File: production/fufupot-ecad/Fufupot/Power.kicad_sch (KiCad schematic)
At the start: 1 part, among them J1 Conn_01x03

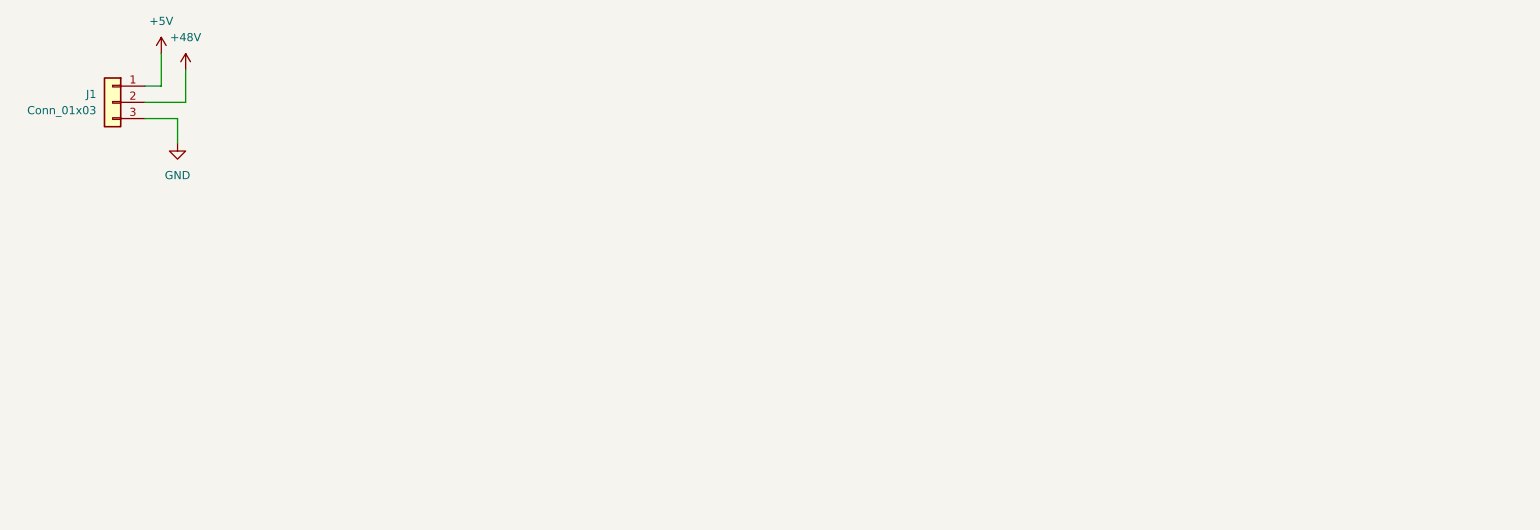
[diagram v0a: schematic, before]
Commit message: Buck Schematic
First version of my buck schematic
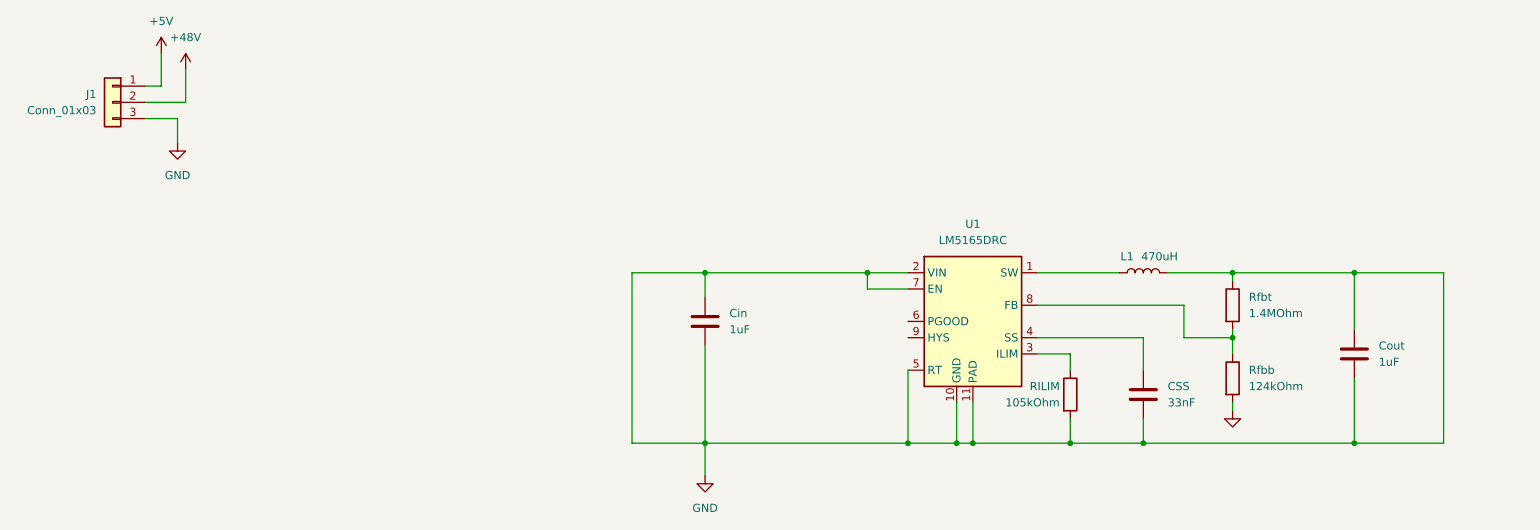
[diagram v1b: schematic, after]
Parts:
- added CSS: 33nF, symbol Device:C
- added Cin, Cout: 1uF, symbol Device:C
- added L1: 470uH, symbol Device:L
- added RILIM: 105kOhm, symbol Device:R
- added Rfbb: 124kOhm, symbol Device:R
- added Rfbt: 1.4MOhm, symbol Device:R
- added U1: LM5165DRC, Package_SON:Texas_S-PVSON-N10_ThermalVias, symbol Regulator_Switching:LM5165
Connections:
- net GND: now also CSS.2, Cin.1, Cin.2, Cout.1, Cout.2, L1.2, RILIM.2, Rfbb.2, Rfbt.1, U1.10 (GND), U1.11 (PAD), U1.2 (VIN), U1.5 (RT), U1.7 (EN)
- new net: L1.1, U1.1 (SW)
- new net: CSS.1, U1.4 (SS)
- new net: Rfbb.1, Rfbt.2, U1.8 (FB)
- new net: RILIM.1, U1.3 (ILIM)

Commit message: Input and Output
Created labels that represent the input 48V from source and where the output 15V should be.
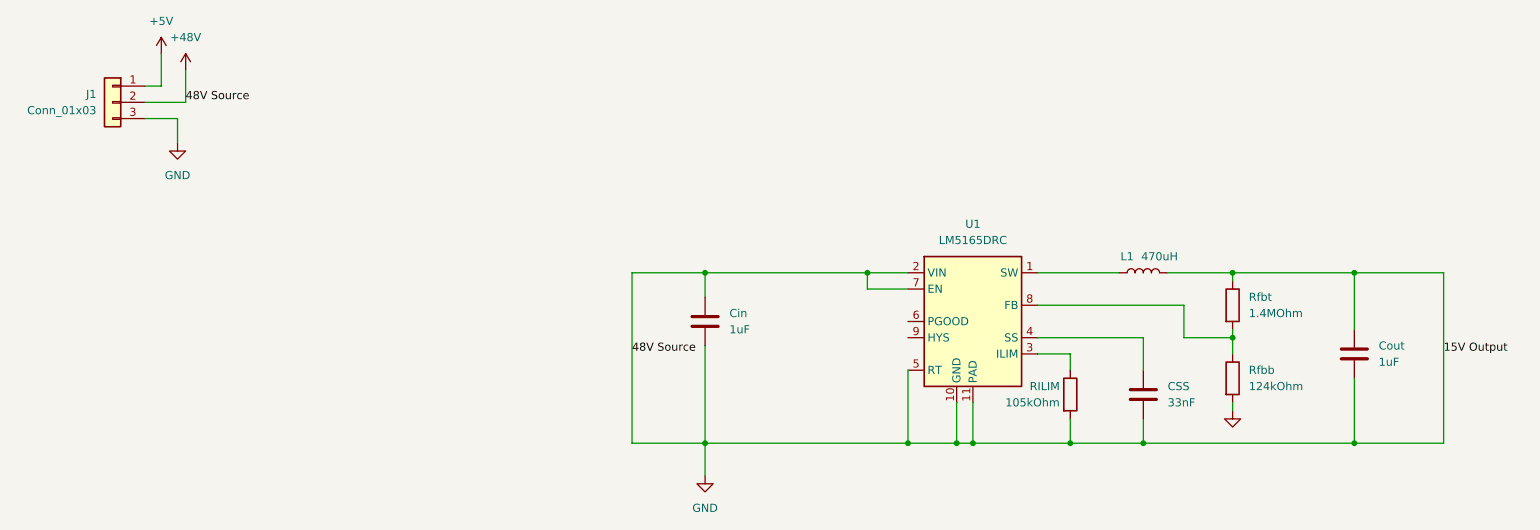
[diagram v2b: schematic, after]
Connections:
- net GND is gone; now on net +48V: CSS.2, Cin.1, Cin.2, Cout.1, Cout.2, J1.3 (Pin_3), L1.2, RILIM.2, Rfbb.2, Rfbt.1, U1.10 (GND), U1.11 (PAD), U1.2 (VIN), U1.5 (RT), U1.7 (EN)
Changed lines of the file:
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@@
+    (stroke (width 0) (type default))
+  )
+  (wire (pts (xy 128.27 68.58) (xy 128.27 95.25))
     (stroke (width 0) (type default))
   )
@@
   )
   (wire (pts (xy 57.15 44.45) (xy 52.07 44.45))
-    (stroke (width 0) (type default))
-  )
-  (wire (pts (xy 128.27 95.25) (xy 128.27 68.58))
     (stroke (width 0) (type default))
   )
@@
     (stroke (width 0) (type default))
   )
+  (label "48V Source" (at 58.42 41.91 0) (fields_autoplaced)
+    (effects (font (size 1.27 1.27)) (justify left bottom))
+  )
+  (label "15V Output" (at 255.27 81.28 0) (fields_autoplaced)
+    (effects (font (size 1.27 1.27)) (justify left bottom))
+  )
+  (label "48V Source" (at 128.27 81.28 0) (fields_autoplaced)
+    (effects (font (size 1.27 1.27)) (justify left bottom))
+  )
   (symbol (lib_id "power:GND") (at 139.7 100.33 0) (unit 1)

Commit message: Last minute changes
Commit with the most recent changes
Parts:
- C3: renamed from Cout; value 1uF -> 10uF
- L1: value 470uH -> 47uH
- R1: renamed from Rfbt; value 1.4MOhm -> 900kOhm
- R2: renamed from Rfbb; value 124kOhm -> 80kOhm
- renumbered Cin to C1, CSS to C2, RILIM to R3
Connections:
- net +48V renamed +15V
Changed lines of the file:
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@@
   (junction (at 241.3 95.25) (diameter 0) (color 0 0 0 0)
   )
+  (junction (at 128.27 68.58) (diameter 0) (color 0 0 0 0)
+  )
   (junction (at 139.7 95.25) (diameter 0) (color 0 0 0 0)
   )
@@
   (junction (at 241.3 68.58) (diameter 0) (color 0 0 0 0)
   )
+  (junction (at 255.27 68.58) (diameter 0) (color 0 0 0 0)
+  )
   (junction (at 222.25 78.74) (diameter 0) (color 0 0 0 0)
   )
@@
     (stroke (width 0) (type default))
   )
+  (wire (pts (xy 128.27 64.77) (xy 128.27 68.58))
+    (stroke (width 0) (type default))
+  )
   (wire (pts (xy 222.25 88.9) (xy 222.25 90.17))
     (stroke (width 0) (type default))
   )
   (wire (pts (xy 208.28 78.74) (xy 208.28 83.82))
+    (stroke (width 0) (type default))
+  )
+  (wire (pts (xy 255.27 64.77) (xy 255.27 68.58))
     (stroke (width 0) (type default))
   )
@@
   (label "48V Source" (at 128.27 81.28 0) (fields_autoplaced)
     (effects (font (size 1.27 1.27)) (justify left bottom))
+  )
+  (symbol (lib_id "power:+15V") (at 255.27 64.77 0) (unit 1)
+    (in_bom yes) (on_board yes) (dnp no) (fields_autoplaced)
+    (property "Reference" "#PWR07" (at 255.27 68.58 0)
+      (effects (font (size 1.27 1.27)) hide)
+    )
+    (property "Value" "+15V" (at 255.27 59.69 0)
+      (effects (font (size 1.27 1.27)))
+    )
+    (property "Footprint" "" (at 255.27 64.77 0)
+      (effects (font (size 1.27 1.27)) hide)
+    )
+    (property "Datasheet" "" (at 255.27 64.77 0)
+      (effects (font (size 1.27 1.27)) hide)
+    )
+    (pin "1")
+    (instances
+      (project "Fufupot"
+        (path "/e8bc21b1-eda8-45a8-be25-55b90339183f/9aa61a69-85f8-4fcb-b123-803352e6223c"
+          (reference "#PWR07") (unit 1)
+        )
+      )
+    )
   )
   (symbol (lib_id "power:GND") (at 139.7 100.33 0) (unit 1)
@@
       (effects (font (size 1.27 1.27)))
     )
-    (property "Value" "470uH" (at 210.82 66.04 90)
+    (property "Value" "47uH" (at 210.82 66.04 90)
       (effects (font (size 1.27 1.27)))
     )
@@
   (symbol (lib_id "Device:C") (at 208.28 87.63 0) (unit 1)
     (in_bom yes) (on_board yes) (dnp no) (fields_autoplaced)
-    (property "Reference" "CSS" (at 212.09 86.36 0)
+    (property "Reference" "C2" (at 212.09 86.36 0)
       (effects (font (size 1.27 1.27)) (justify left))
     )
@@
       (project "Fufupot"
         (path "/e8bc21b1-eda8-45a8-be25-55b90339183f/9aa61a69-85f8-4fcb-b123-803352e6223c"
-          (reference "CSS") (unit 1)
+          (reference "C2") (unit 1)
         )
       )
@@
   (symbol (lib_id "Device:R") (at 222.25 73.66 0) (unit 1)
     (in_bom yes) (on_board yes) (dnp no) (fields_autoplaced)
-    (property "Reference" "Rfbt" (at 224.79 72.39 0)
-      (effects (font (size 1.27 1.27)) (justify left))
-    )
-    (property "Value" "1.4MOhm" (at 224.79 74.93 0)
+    (property "Reference" "R1" (at 224.79 72.39 0)
+      (effects (font (size 1.27 1.27)) (justify left))
+    )
+    (property "Value" "900kOhm" (at 224.79 74.93 0)
       (effects (font (size 1.27 1.27)) (justify left))
     )
@@
       (project "Fufupot"
         (path "/e8bc21b1-eda8-45a8-be25-55b90339183f/9aa61a69-85f8-4fcb-b123-803352e6223c"
-          (reference "Rfbt") (unit 1)
+          (reference "R1") (unit 1)
+        )
+      )
+    )
+  )
+  (symbol (lib_id "power:+48V") (at 128.27 64.77 0) (unit 1)
+    (in_bom yes) (on_board yes) (dnp no) (fields_autoplaced)
+    (property "Reference" "#PWR06" (at 128.27 68.58 0)
+      (effects (font (size 1.27 1.27)) hide)
+    )
+    (property "Value" "+48V" (at 128.27 59.69 0)
+      (effects (font (size 1.27 1.27)))
+    )
+    (property "Footprint" "" (at 128.27 64.77 0)
+      (effects (font (size 1.27 1.27)) hide)
+    )
+    (property "Datasheet" "" (at 128.27 64.77 0)
+      (effects (font (size 1.27 1.27)) hide)
+    )
+    (pin "1")
+    (instances
+      (project "Fufupot"
+        (path "/e8bc21b1-eda8-45a8-be25-55b90339183f/9aa61a69-85f8-4fcb-b123-803352e6223c"
+          (reference "#PWR06") (unit 1)
         )
       )
@@
   (symbol (lib_id "Device:R") (at 222.25 85.09 0) (unit 1)
     (in_bom yes) (on_board yes) (dnp no) (fields_autoplaced)
-    (property "Reference" "Rfbb" (at 224.79 83.82 0)
-      (effects (font (size 1.27 1.27)) (justify left))
-    )
-    (property "Value" "124kOhm" (at 224.79 86.36 0)
+    (property "Reference" "R2" (at 224.79 83.82 0)
+      (effects (font (size 1.27 1.27)) (justify left))
+    )
+    (property "Value" "80kOhm" (at 224.79 86.36 0)
       (effects (font (size 1.27 1.27)) (justify left))
     )
@@
       (project "Fufupot"
         (path "/e8bc21b1-eda8-45a8-be25-55b90339183f/9aa61a69-85f8-4fcb-b123-803352e6223c"
-          (reference "Rfbb") (unit 1)
+          (reference "R2") (unit 1)
         )
       )
@@
   (symbol (lib_id "Device:C") (at 241.3 81.28 0) (unit 1)
     (in_bom yes) (on_board yes) (dnp no) (fields_autoplaced)
-    (property "Reference" "Cout" (at 245.11 80.01 0)
-      (effects (font (size 1.27 1.27)) (justify left))
-    )
-    (property "Value" "1uF" (at 245.11 82.55 0)
+    (property "Reference" "C3" (at 245.11 80.01 0)
+      (effects (font (size 1.27 1.27)) (justify left))
+    )
+    (property "Value" "10uF" (at 245.11 82.55 0)
       (effects (font (size 1.27 1.27)) (justify left))
     )
@@
       (project "Fufupot"
         (path "/e8bc21b1-eda8-45a8-be25-55b90339183f/9aa61a69-85f8-4fcb-b123-803352e6223c"
-          (reference "Cout") (unit 1)
+          (reference "C3") (unit 1)
         )
       )
@@
   (symbol (lib_id "Device:R") (at 196.85 87.63 0) (unit 1)
     (in_bom yes) (on_board yes) (dnp no)
-    (property "Reference" "RILIM" (at 190.5 86.36 0)
+    (property "Reference" "R3" (at 190.5 86.36 0)
       (effects (font (size 1.27 1.27)) (justify left))
     )
@@
       (project "Fufupot"
         (path "/e8bc21b1-eda8-45a8-be25-55b90339183f/9aa61a69-85f8-4fcb-b123-803352e6223c"
-          (reference "RILIM") (unit 1)
+          (reference "R3") (unit 1)
         )
       )
@@
   (symbol (lib_id "Device:C") (at 139.7 76.2 0) (unit 1)
     (in_bom yes) (on_board yes) (dnp no) (fields_autoplaced)
-    (property "Reference" "Cin" (at 143.51 74.93 0)
+    (property "Reference" "C1" (at 143.51 74.93 0)
       (effects (font (size 1.27 1.27)) (justify left))
     )
@@
       (project "Fufupot"
         (path "/e8bc21b1-eda8-45a8-be25-55b90339183f/9aa61a69-85f8-4fcb-b123-803352e6223c"
-          (reference "Cin") (unit 1)
-        )
-      )
+          (reference "C1") (unit 1)
+        )
+      )
